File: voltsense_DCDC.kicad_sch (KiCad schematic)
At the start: 9 parts, among them J16 Capacitor connector, U8 Opamp_Quad

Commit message: SCH Save: 3 files changed currsense_DCDC.kicad_sch 0/216/282 voltsense_DCDC.kicad_sch 0/220/295 WET_PCB_v2.kicad_pro 0/0/1
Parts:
- removed U8: Opamp_Quad, symbol Device:Opamp_Quad
- added U3: TLV9301xDCK, Package_TO_SOT_SMD:SOT-353_SC-70-5, symbol Amplifier_Operational:TLV9301xDCK
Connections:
- net GND: now also U3.2 (V-)
- net VDD_OPAMP: now also U3.5 (V+)
- net at R4.1: now also U3.3 (-), U3.4
- net at R3.2: now also U3.1 (+)
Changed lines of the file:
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@@
+	(wire
+		(pts
+			(xy 87.63 38.1) (xy 87.63 43.18)
+		)
+		(stroke
+			(width 0)
+			(type default)
+		)
+	)
+	(wire
+		(pts
+			(xy 87.63 58.42) (xy 87.63 59.69)
+		)
+		(stroke
+			(width 0)
+			(type default)
+		)
+	)
 	(wire
 		(pts
@@
 	(label "VDD_OPAMP"
 		(at 128.27 38.1 0)
+		(effects
+			(font
+				(size 1.27 1.27)
+			)
+			(justify left bottom)
+		)
+	)
+	(label "VDD_OPAMP"
+		(at 87.63 38.1 0)
 		(effects
 			(font
@@
 	)
 	(symbol
-		(lib_id "Device:Opamp_Quad")
-		(at 90.17 50.8 0)
-		(unit 1)
-		(body_style 1)
-		(exclude_from_sim no)
-		(in_bom yes)
-		(on_board yes)
-		(in_pos_files yes)
-		(dnp no)
-		(fields_autoplaced yes)
-		(property "Reference" "U8"
-			(at 90.17 40.64 0)
-			(show_name no)
-			(do_not_autoplace no)
-			(effects
-				(font
-					(size 1.27 1.27)
-				)
-			)
-		)
-		(property "Value" "Opamp_Quad"
-			(at 90.17 43.18 0)
-			(show_name no)
-			(do_not_autoplace no)
-			(effects
-				(font
-					(size 1.27 1.27)
-				)
-			)
-		)
-		(property "Footprint" ""
-			(at 90.17 50.8 0)
-			(hide yes)
-			(show_name no)
-			(do_not_autoplace no)
-			(effects
-				(font
-					(size 1.27 1.27)
-				)
-			)
-		)
-		(property "Datasheet" ""
-			(at 90.17 50.8 0)
-			(hide yes)
-			(show_name no)
-			(do_not_autoplace no)
-			(effects
-				(font
-					(size 1.27 1.27)
-				)
-			)
-		)
-		(property "Description" "Quad operational amplifier"
-			(at 90.17 50.8 0)
-			(hide yes)
-			(show_name no)
-			(do_not_autoplace no)
-			(effects
-				(font
-					(size 1.27 1.27)
-				)
-			)
-		)
-		(property "Sim.Library" "${KICAD9_SYMBOL_DIR}/Simulation_SPICE.sp"
-			(at 90.17 50.8 0)
-			(hide yes)
-			(show_name no)
-			(do_not_autoplace no)
-			(effects
-				(font
-					(size 1.27 1.27)
-				)
-			)
-		)
-		(property "Sim.Name" "kicad_builtin_opamp_quad"
-			(at 90.17 50.8 0)
-			(hide yes)
-			(show_name no)
-			(do_not_autoplace no)
-			(effects
-				(font
-					(size 1.27 1.27)
-				)
-			)
-		)
-		(property "Sim.Device" "SUBCKT"
-			(at 90.17 50.8 0)
-			(hide yes)
-			(show_name no)
-			(do_not_autoplace no)
-			(effects
-				(font
-					(size 1.27 1.27)
-				)
-			)
-		)
-		(property "Sim.Pins" "1=out1 2=in1- 3=in1+ 4=vcc 5=in2+ 6=in2- 7=out2 8=out3 9=in3- 10=in3+ 11=vee 12=in4+ 13=in4- 14=out4"
-			(at 90.17 50.8 0)
-			(hide yes)
-			(show_name no)
-			(do_not_autoplace no)
-			(effects
-				(font
-					(size 1.27 1.27)
-				)
-			)
-		)
-		(pin "6"
-		)
-		(pin "9"
-		)
-		(pin "5"
-		)
-		(pin "11"
-		)
-		(pin "12"
-		)
-		(pin "10"
-		)
-		(pin "13"
-		)
-		(pin "2"
-		)
-		(pin "1"
-		)
-		(pin "14"
-		)
-		(pin "4"
-		)
-		(pin "3"
-		)
-		(pin "8"
-		)
-		(pin "7"
-		)
-		(instances
-			(project "WET_PCB_v2"
-				(path "/13451c35-1666-47d9-9525-8d8125ba1cf3/a17383a4-d27f-4c25-9e0c-b0df1856b8d8"
-					(reference "U8")
-					(unit 1)
-				)
-			)
-		)
-	)
-	(symbol
 		(lib_id "power:GND")
 		(at 53.34 59.69 0)
@@
 				(path "/13451c35-1666-47d9-9525-8d8125ba1cf3/a17383a4-d27f-4c25-9e0c-b0df1856b8d8"
 					(reference "#PWR017")
+					(unit 1)
+				)
+			)
+		)
+	)
+	(symbol
+		(lib_id "Amplifier_Operational:TLV9301xDCK")
+		(at 87.63 50.8 0)
+		(unit 1)
+		(body_style 1)
+		(exclude_from_sim no)
+		(in_bom yes)
+		(on_board yes)
+		(in_pos_files yes)
+		(dnp no)
+		(fields_autoplaced yes)
+		(property "Reference" "U3"
+			(at 102.87 44.3798 0)
+			(show_name no)
+			(do_not_autoplace no)
+			(effects
+				(font
+					(size 1.27 1.27)
+				)
+			)
+		)
+		(property "Value" "TLV9301xDCK"
+			(at 102.87 46.9198 0)
+			(show_name no)
+			(do_not_autoplace no)
+			(effects
+				(font
+					(size 1.27 1.27)
+				)
+			)
+		)
+		(property "Footprint" "Package_TO_SOT_SMD:SOT-353_SC-70-5"
+			(at 92.71 50.8 0)
+			(hide yes)
+			(show_name no)
+			(do_not_autoplace no)
+			(effects
+				(font
+					(size 1.27 1.27)
+				)
+			)
+		)
+		(property "Datasheet" "https://www.ti.com/lit/ds/symlink/tlv9301.pdf"
+			(at 87.63 50.8 0)
+			(hide yes)
+			(show_name no)
+			(do_not_autoplace no)
+			(effects
+				(font
+					(size 1.27 1.27)
+				)
+			)
+		)
+		(property "Description" "40-V, 1-MHz, RRO Operational Amplifiers for Cost-Sensitive Systems, SC-70"
+			(at 87.63 50.8 0)
+			(hide yes)
+			(show_name no)
+			(do_not_autoplace no)
+			(effects
+				(font
+					(size 1.27 1.27)
+				)
+			)
+		)
+		(pin "1"
+		)
+		(pin "2"
+		)
+		(pin "3"
+		)
+		(pin "4"
+		)
+		(pin "5"
+		)
+		(instances
+			(project "WET_PCB_v2"
+				(path "/13451c35-1666-47d9-9525-8d8125ba1cf3/a17383a4-d27f-4c25-9e0c-b0df1856b8d8"
+					(reference "U3")
 					(unit 1)
 				)
@@
 					(unit 1)
 				)
+			)
+		)
+	)
+	(symbol
+		(lib_id "power:GND")
+		(at 87.63 59.69 0)
+		(unit 1)
+		(body_style 1)
+		(exclude_from_sim no)
+		(in_bom yes)
+		(on_board yes)
+		(in_pos_files yes)
+		(dnp no)
+		(fields_autoplaced yes)
+		(property "Reference" "#PWR020"
+			(at 87.63 66.04 0)
+			(hide yes)
+			(show_name no)
+			(do_not_autoplace no)
+			(effects
+				(font
+					(size 1.27 1.27)
+				)
+			)
+		)
+		(property "Value" "GND"
+			(at 87.63 64.77 0)
+			(show_name no)
+			(do_not_autoplace no)
+			(effects
+				(font
+					(size 1.27 1.27)
+				)
+			)
+		)
+		(property "Footprint" ""
+			(at 87.63 59.69 0)
+			(hide yes)
+			(show_name no)
+			(do_not_autoplace no)
+			(effects
+				(font
+					(size 1.27 1.27)
+				)
+			)
+		)
+		(property "Datasheet" ""
+			(at 87.63 59.69 0)
+			(hide yes)
+			(show_name no)
+			(do_not_autoplace no)
+			(effects
+				(font
+					(size 1.27 1.27)
+				)
+			)
+		)
+		(property "Description" "Power symbol creates a global label with name \"GND\" , ground"
+			(at 87.63 59.69 0)
+			(hide yes)
+			(show_name no)
+			(do_not_autoplace no)
+			(effects
+				(font
+					(size 1.27 1.27)
+				)
+			)
+		)
+		(pin "1"
+		)
+		(instances
+			(project "WET_PCB_v2"
+				(path "/13451c35-1666-47d9-9525-8d8125ba1cf3/a17383a4-d27f-4c25-9e0c-b0df1856b8d8"
+					(reference "#PWR020")
+					(unit 1)
+				)

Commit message: SCH Save: 1 files changed voltsense_DCDC.kicad_sch 220/0/295
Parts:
- removed U3: TLV9301xDCK, Package_TO_SOT_SMD:SOT-353_SC-70-5, symbol Amplifier_Operational:TLV9301xDCK
- added U8: Opamp_Quad, symbol Device:Opamp_Quad
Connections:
- net at R3.2: now also U8.3 (+)
- net at R4.1: now also U8.1, U8.2 (-)
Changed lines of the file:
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@@
 	(wire
 		(pts
-			(xy 87.63 38.1) (xy 87.63 43.18)
+			(xy 128.27 63.5) (xy 128.27 59.69)
 		)
 		(stroke
@@
 	(wire
 		(pts
-			(xy 87.63 58.42) (xy 87.63 59.69)
+			(xy 97.79 50.8) (xy 97.79 67.31)
 		)
 		(stroke
@@
 	(wire
 		(pts
-			(xy 128.27 63.5) (xy 128.27 59.69)
+			(xy 76.2 20.32) (xy 73.66 20.32)
 		)
 		(stroke
@@
 		)
 	)
-	(wire
-		(pts
-			(xy 97.79 50.8) (xy 97.79 67.31)
-		)
-		(stroke
-			(width 0)
-			(type default)
-		)
-	)
-	(wire
-		(pts
-			(xy 76.2 20.32) (xy 73.66 20.32)
-		)
-		(stroke
-			(width 0)
-			(type default)
-		)
-	)
 	(label "VDD_OPAMP"
 		(at 128.27 38.1 0)
-		(effects
-			(font
-				(size 1.27 1.27)
-			)
-			(justify left bottom)
-		)
-	)
-	(label "VDD_OPAMP"
-		(at 87.63 38.1 0)
 		(effects
 			(font
@@
 	)
 	(symbol
+		(lib_id "Device:Opamp_Quad")
+		(at 90.17 50.8 0)
+		(unit 1)
+		(body_style 1)
+		(exclude_from_sim no)
+		(in_bom yes)
+		(on_board yes)
+		(in_pos_files yes)
+		(dnp no)
+		(fields_autoplaced yes)
+		(property "Reference" "U8"
+			(at 90.17 40.64 0)
+			(show_name no)
+			(do_not_autoplace no)
+			(effects
+				(font
+					(size 1.27 1.27)
+				)
+			)
+		)
+		(property "Value" "Opamp_Quad"
+			(at 90.17 43.18 0)
+			(show_name no)
+			(do_not_autoplace no)
+			(effects
+				(font
+					(size 1.27 1.27)
+				)
+			)
+		)
+		(property "Footprint" ""
+			(at 90.17 50.8 0)
+			(hide yes)
+			(show_name no)
+			(do_not_autoplace no)
+			(effects
+				(font
+					(size 1.27 1.27)
+				)
+			)
+		)
+		(property "Datasheet" ""
+			(at 90.17 50.8 0)
+			(hide yes)
+			(show_name no)
+			(do_not_autoplace no)
+			(effects
+				(font
+					(size 1.27 1.27)
+				)
+			)
+		)
+		(property "Description" "Quad operational amplifier"
+			(at 90.17 50.8 0)
+			(hide yes)
+			(show_name no)
+			(do_not_autoplace no)
+			(effects
+				(font
+					(size 1.27 1.27)
+				)
+			)
+		)
+		(property "Sim.Library" "${KICAD9_SYMBOL_DIR}/Simulation_SPICE.sp"
+			(at 90.17 50.8 0)
+			(hide yes)
+			(show_name no)
+			(do_not_autoplace no)
+			(effects
+				(font
+					(size 1.27 1.27)
+				)
+			)
+		)
+		(property "Sim.Name" "kicad_builtin_opamp_quad"
+			(at 90.17 50.8 0)
+			(hide yes)
+			(show_name no)
+			(do_not_autoplace no)
+			(effects
+				(font
+					(size 1.27 1.27)
+				)
+			)
+		)
+		(property "Sim.Device" "SUBCKT"
+			(at 90.17 50.8 0)
+			(hide yes)
+			(show_name no)
+			(do_not_autoplace no)
+			(effects
+				(font
+					(size 1.27 1.27)
+				)
+			)
+		)
+		(property "Sim.Pins" "1=out1 2=in1- 3=in1+ 4=vcc 5=in2+ 6=in2- 7=out2 8=out3 9=in3- 10=in3+ 11=vee 12=in4+ 13=in4- 14=out4"
+			(at 90.17 50.8 0)
+			(hide yes)
+			(show_name no)
+			(do_not_autoplace no)
+			(effects
+				(font
+					(size 1.27 1.27)
+				)
+			)
+		)
+		(pin "6"
+		)
+		(pin "9"
+		)
+		(pin "5"
+		)
+		(pin "11"
+		)
+		(pin "12"
+		)
+		(pin "10"
+		)
+		(pin "13"
+		)
+		(pin "2"
+		)
+		(pin "1"
+		)
+		(pin "14"
+		)
+		(pin "4"
+		)
+		(pin "3"
+		)
+		(pin "8"
+		)
+		(pin "7"
+		)
+		(instances
+			(project "WET_PCB_v2"
+				(path "/13451c35-1666-47d9-9525-8d8125ba1cf3/a17383a4-d27f-4c25-9e0c-b0df1856b8d8"
+					(reference "U8")
+					(unit 1)
+				)
+			)
+		)
+	)
+	(symbol
 		(lib_id "power:GND")
 		(at 53.34 59.69 0)
@@
 				(path "/13451c35-1666-47d9-9525-8d8125ba1cf3/a17383a4-d27f-4c25-9e0c-b0df1856b8d8"
 					(reference "#PWR017")
-					(unit 1)
-				)
-			)
-		)
-	)
-	(symbol
-		(lib_id "Amplifier_Operational:TLV9301xDCK")
-		(at 87.63 50.8 0)
-		(unit 1)
-		(body_style 1)
-		(exclude_from_sim no)
-		(in_bom yes)
-		(on_board yes)
-		(in_pos_files yes)
-		(dnp no)
-		(fields_autoplaced yes)
-		(property "Reference" "U3"
-			(at 102.87 44.3798 0)
-			(show_name no)
-			(do_not_autoplace no)
-			(effects
-				(font
-					(size 1.27 1.27)
-				)
-			)
-		)
-		(property "Value" "TLV9301xDCK"
-			(at 102.87 46.9198 0)
-			(show_name no)
-			(do_not_autoplace no)
-			(effects
-				(font
-					(size 1.27 1.27)
-				)
-			)
-		)
-		(property "Footprint" "Package_TO_SOT_SMD:SOT-353_SC-70-5"
-			(at 92.71 50.8 0)
-			(hide yes)
-			(show_name no)
-			(do_not_autoplace no)
-			(effects
-				(font
-					(size 1.27 1.27)
-				)
-			)
-		)
-		(property "Datasheet" "https://www.ti.com/lit/ds/symlink/tlv9301.pdf"
-			(at 87.63 50.8 0)
-			(hide yes)
-			(show_name no)
-			(do_not_autoplace no)
-			(effects
-				(font
-					(size 1.27 1.27)
-				)
-			)
-		)
-		(property "Description" "40-V, 1-MHz, RRO Operational Amplifiers for Cost-Sensitive Systems, SC-70"
-			(at 87.63 50.8 0)
-			(hide yes)
-			(show_name no)
-			(do_not_autoplace no)
-			(effects
-				(font
-					(size 1.27 1.27)
-				)
-			)
-		)
-		(pin "1"
-		)
-		(pin "2"
-		)
-		(pin "3"
-		)
-		(pin "4"
-		)
-		(pin "5"
-		)
-		(instances
-			(project "WET_PCB_v2"
-				(path "/13451c35-1666-47d9-9525-8d8125ba1cf3/a17383a4-d27f-4c25-9e0c-b0df1856b8d8"
-					(reference "U3")
 					(unit 1)
 				)
@@
 					(unit 1)
 				)
-			)
-		)
-	)
-	(symbol
-		(lib_id "power:GND")
-		(at 87.63 59.69 0)
-		(unit 1)
-		(body_style 1)
-		(exclude_from_sim no)
-		(in_bom yes)
-		(on_board yes)
-		(in_pos_files yes)
-		(dnp no)
-		(fields_autoplaced yes)
-		(property "Reference" "#PWR020"
-			(at 87.63 66.04 0)
-			(hide yes)
-			(show_name no)
-			(do_not_autoplace no)
-			(effects
-				(font
-					(size 1.27 1.27)
-				)
-			)
-		)
-		(property "Value" "GND"
-			(at 87.63 64.77 0)
-			(show_name no)
-			(do_not_autoplace no)
-			(effects
-				(font
-					(size 1.27 1.27)
-				)
-			)
-		)
-		(property "Footprint" ""
-			(at 87.63 59.69 0)
-			(hide yes)
-			(show_name no)
-			(do_not_autoplace no)
-			(effects
-				(font
-					(size 1.27 1.27)
-				)
-			)
-		)
-		(property "Datasheet" ""
-			(at 87.63 59.69 0)
-			(hide yes)
-			(show_name no)
-			(do_not_autoplace no)
-			(effects
-				(font
-					(size 1.27 1.27)
-				)
-			)
-		)
-		(property "Description" "Power symbol creates a global label with name \"GND\" , ground"
-			(at 87.63 59.69 0)
-			(hide yes)
-			(show_name no)
-			(do_not_autoplace no)
-			(effects
-				(font
-					(size 1.27 1.27)
-				)
-			)
-		)
-		(pin "1"
-		)
-		(instances
-			(project "WET_PCB_v2"
-				(path "/13451c35-1666-47d9-9525-8d8125ba1cf3/a17383a4-d27f-4c25-9e0c-b0df1856b8d8"
-					(reference "#PWR020")
-					(unit 1)
-				)

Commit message: SCH Save: 1 files changed voltsense_DCDC.kicad_sch 0/0/2
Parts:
- renumbered U8 to U3
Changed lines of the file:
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@@
 		(dnp no)
 		(fields_autoplaced yes)
-		(property "Reference" "U8"
+		(property "Reference" "U3"
 			(at 90.17 40.64 0)
 			(show_name no)
@@
 			(project "WET_PCB_v2"
 				(path "/13451c35-1666-47d9-9525-8d8125ba1cf3/a17383a4-d27f-4c25-9e0c-b0df1856b8d8"
-					(reference "U8")
+					(reference "U3")
 					(unit 1)
 				)

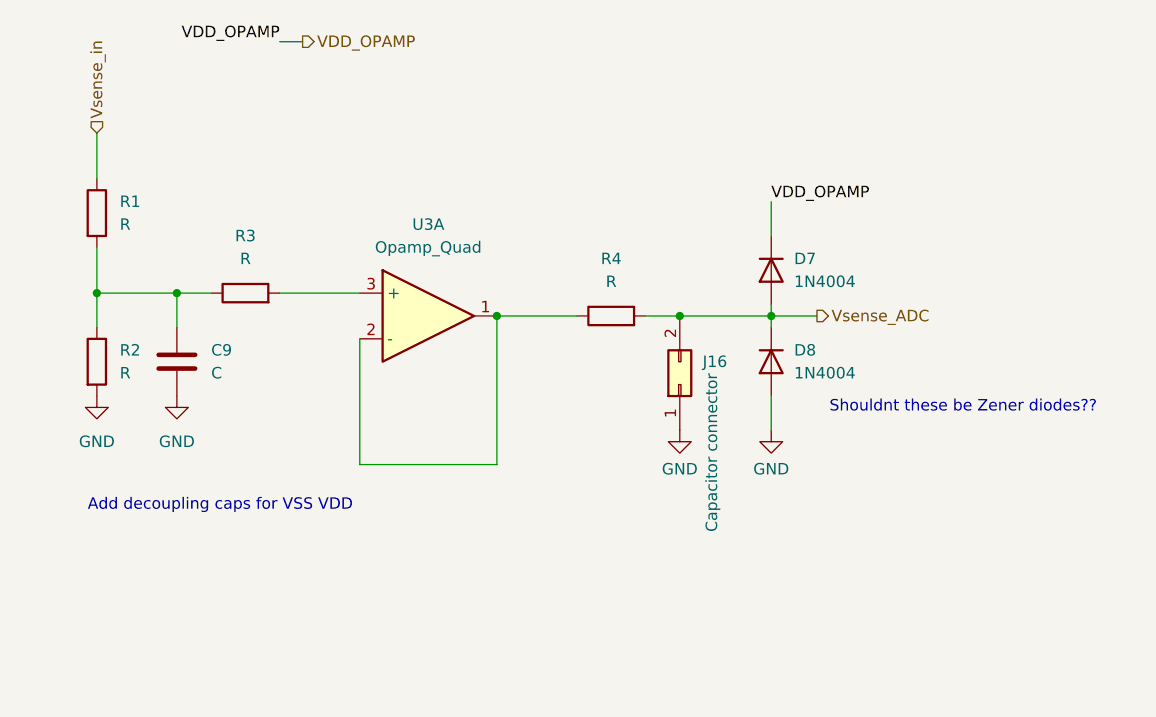
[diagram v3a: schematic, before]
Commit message: SCH Save: 1 files changed voltsense_DCDC.kicad_sch 0/10/351
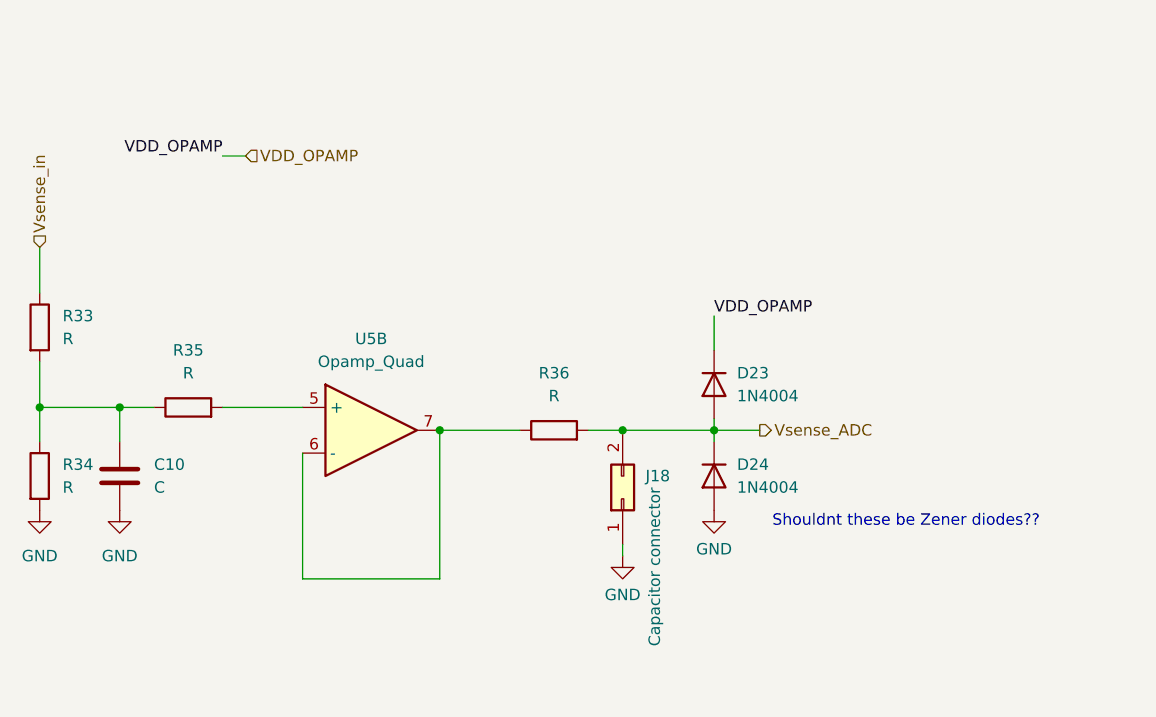
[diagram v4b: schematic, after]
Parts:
- removed C9: C, symbol Device:C
- removed D7, D8: 1N4004, Diode_THT:D_DO-41_SOD81_P10.16mm_Horizontal, symbol Diode:1N4004
- removed J16: Capacitor connector, symbol Connector_Generic:Conn_02x01
- removed R1, R2, R3, R4: R, symbol Device:R
- removed U3: Opamp_Quad, symbol Device:Opamp_Quad
- added C10: C, symbol Device:C
- added D23, D24: 1N4004, Diode_THT:D_DO-41_SOD81_P10.16mm_Horizontal, symbol Diode:1N4004
- added J18: Capacitor connector, symbol Connector_Generic:Conn_02x01
- added R33, R34, R35, R36: R, symbol Device:R
- added U5: Opamp_Quad, symbol Device:Opamp_Quad
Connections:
- net GND: now also C10.2, D24.2 (A), J18.1 (Pin_1), R34.2
- net VDD_OPAMP: now also D23.1 (K)
- net Vsense_ADC: now also D23.2 (A), D24.1 (K), J18.2 (Pin_2), R36.2
- net Vsense_in: now also R33.1
- new net: C10.1, R33.2, R34.1, R35.1
- new net: R35.2, U5.5 (+)
- new net: R36.1, U5.6 (-), U5.7
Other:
- note removed: "Add decoupling caps for VSS VDD"
